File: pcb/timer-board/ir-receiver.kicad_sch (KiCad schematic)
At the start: 1 part, among them U2 TSSP58038

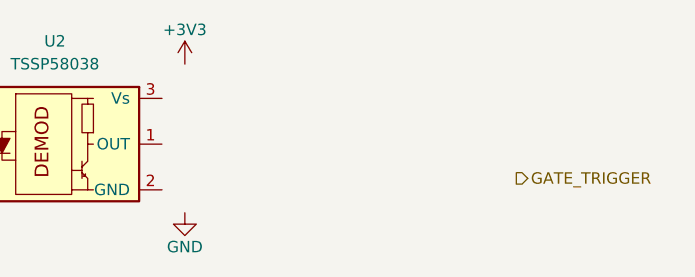
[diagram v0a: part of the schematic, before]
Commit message: Layout power planes and different signals
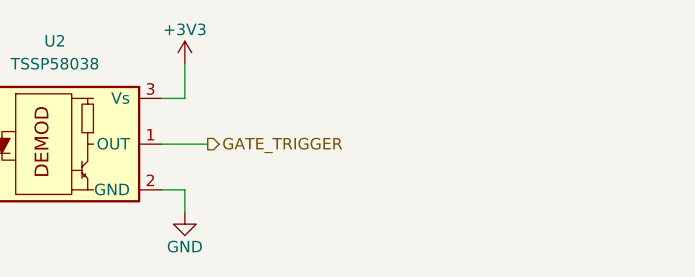
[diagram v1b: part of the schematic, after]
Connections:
- net +3V3: now also U2.3 (Vs)
- net GATE_TRIGGER: now also U2.1 (OUT)
- net GND: now also U2.2 (GND)
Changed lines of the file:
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@@
 		(comment 1 "Project author: Dominik Pluta")
+	)
+	(wire
+		(pts
+			(xy 148.59 95.25) (xy 153.67 95.25)
+		)
+		(stroke
+			(width 0)
+			(type default)
+		)
+	)
+	(wire
+		(pts
+			(xy 151.13 102.87) (xy 151.13 100.33)
+		)
+		(stroke
+			(width 0)
+			(type default)
+		)
+	)
+	(wire
+		(pts
+			(xy 151.13 100.33) (xy 148.59 100.33)
+		)
+		(stroke
+			(width 0)
+			(type default)
+		)
+	)
+	(wire
+		(pts
+			(xy 148.59 90.17) (xy 151.13 90.17)
+		)
+		(stroke
+			(width 0)
+			(type default)
+		)
+	)
+	(wire
+		(pts
+			(xy 151.13 90.17) (xy 151.13 86.36)
+		)
+		(stroke
+			(width 0)
+			(type default)
+		)
 	)
 	(hierarchical_label "GATE_TRIGGER"
 		(shape output)
-		(at 187.96 99.06 0)
+		(at 153.67 95.25 0)
 		(effects
 			(font

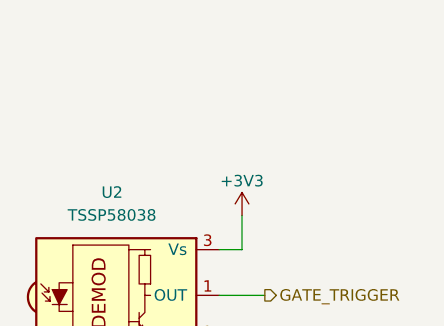
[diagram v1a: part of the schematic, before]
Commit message: Finish uncompleted schematic sections, layout most of the PCB
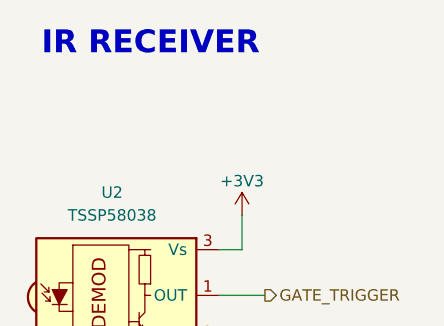
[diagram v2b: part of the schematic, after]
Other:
- note added: "IR RECEIVER"
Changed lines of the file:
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@@
 		(comment 1 "Project author: Dominik Pluta")
+	)
+	(text "IR RECEIVER"
+		(exclude_from_sim no)
+		(at 140.97 67.31 0)
+		(effects
+			(font
+				(size 2.54 2.54)
+				(thickness 0.508)
+				(bold yes)
+			)
+		)
 	)
 	(wire

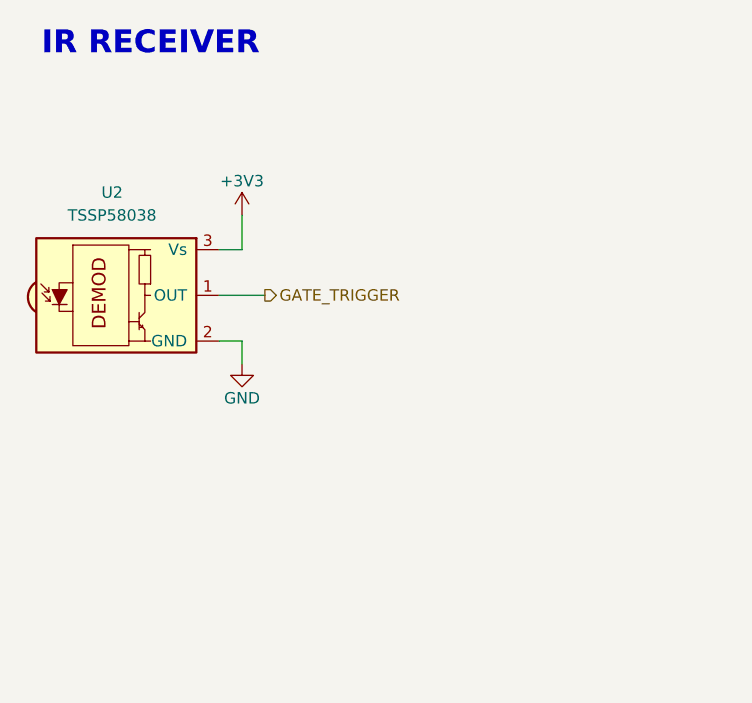
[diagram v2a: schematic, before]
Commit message: Add 3.5mm jack, fix BOOT0 connection
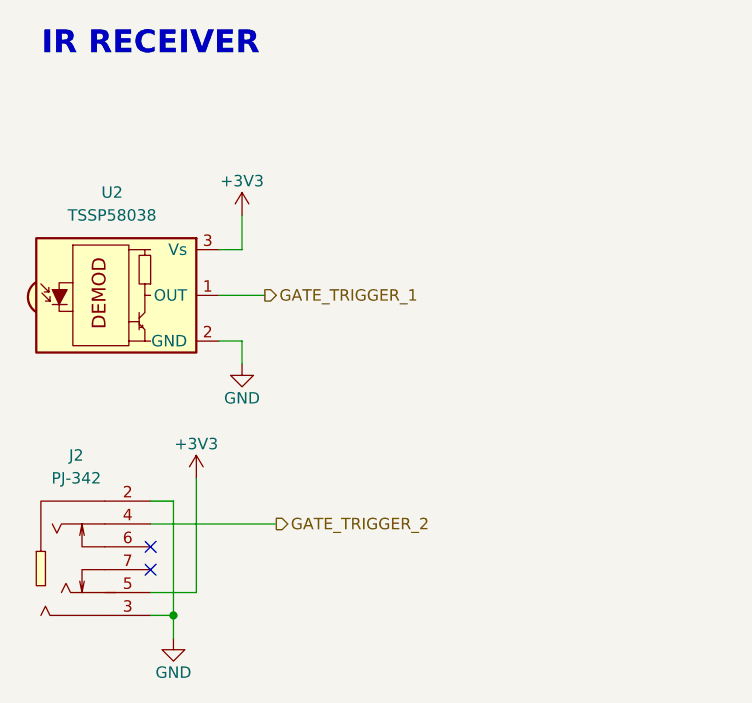
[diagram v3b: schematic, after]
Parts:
- added J2: Jack_PJ-342, DW-footprints:Jack_PJ-342, symbol DW-connectors:Jack_PJ-342
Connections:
- net +3V3: now also J2.5
- net GND: now also J2.2, J2.3
- net GATE_TRIGGER renamed GATE_TRIGGER_1
- new net GATE_TRIGGER_2: J2.4
- no-connect marks 0 -> 2

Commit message: Add I2C pull-up, IR receiver decoupling, LED labels, clear ERC and DRC
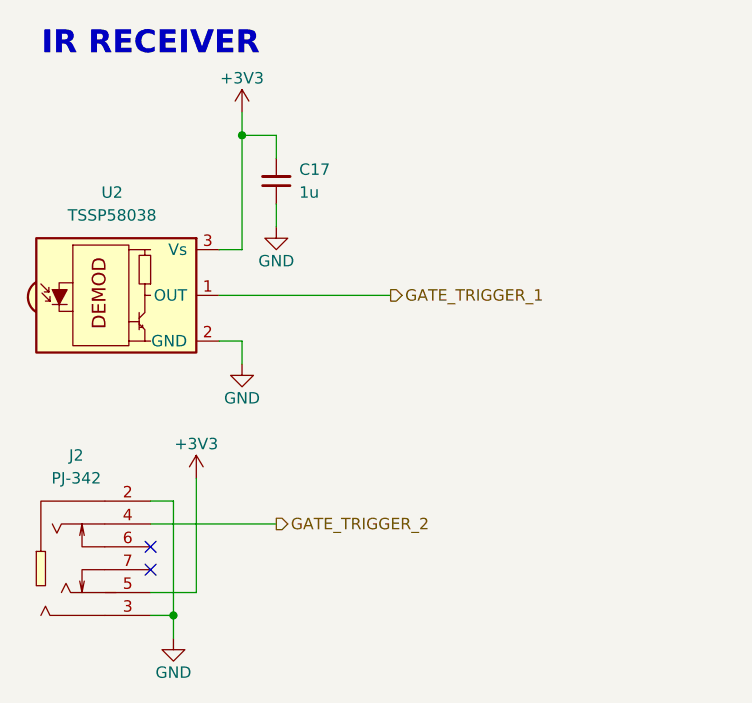
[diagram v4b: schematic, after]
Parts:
- added C17: C-1u-0402, DW-footprints:C_0402_1005Metric, symbol DW-capacitors:C-1u-0402
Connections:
- net +3V3: now also C17.2
- net GND: now also C17.1
